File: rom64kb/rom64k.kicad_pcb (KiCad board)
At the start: 2 copper layers, 81.3 x 65.3 mm, 3 parts, among them P1 CONN_02X25, U2 SST39SF010

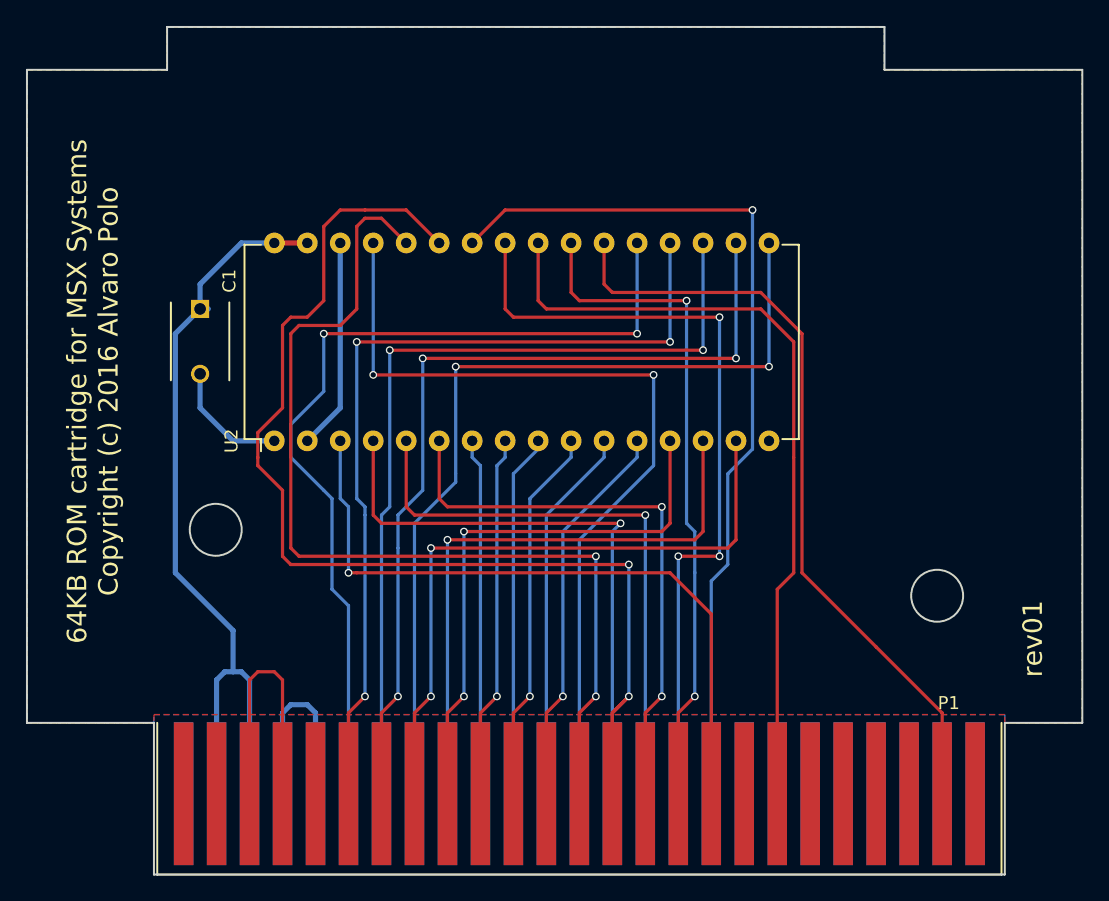
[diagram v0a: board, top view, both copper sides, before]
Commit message: upd: update PCB designs to KiCAD 8
- rom-burner: Update libraries
- rom-burner: Re-routed some paths to improve thermal reliefs in GND
  pads and avoid isolated islands
- rom64kb: Re-routed some paths to avoid isolated islands
- rom64kb: Removed solder mask in golden fingers area
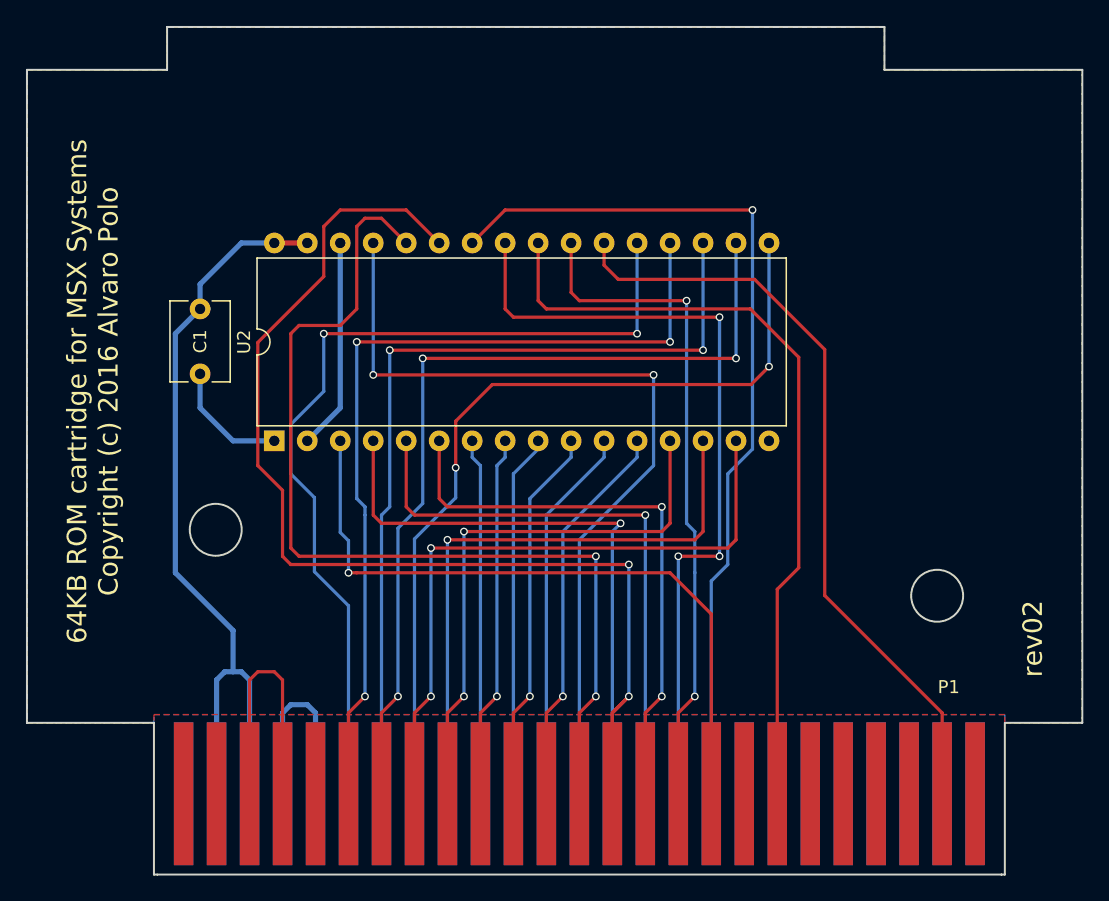
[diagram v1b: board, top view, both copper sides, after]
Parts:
- C1: footprint Capacitors_ThroughHole:C_Disc_D6_P5 -> Capacitor_THT:C_Disc_D6.0mm_W4.4mm_P5.00mm
- U2: footprint Housings_DIP:DIP-32_W15.24mm -> Package_DIP:DIP-32_W15.24mm
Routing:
- net /D3: track 67.9 -> 65.4 mm
- net /A8: track 92.6 -> 91.9 mm
- net ~{SLTSL}: track 59.9 -> 59.4 mm
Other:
- board text added: "rev02"
- board text removed: "rev01"
